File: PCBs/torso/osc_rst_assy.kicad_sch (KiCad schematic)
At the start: 8 parts, among them SW1 RESET

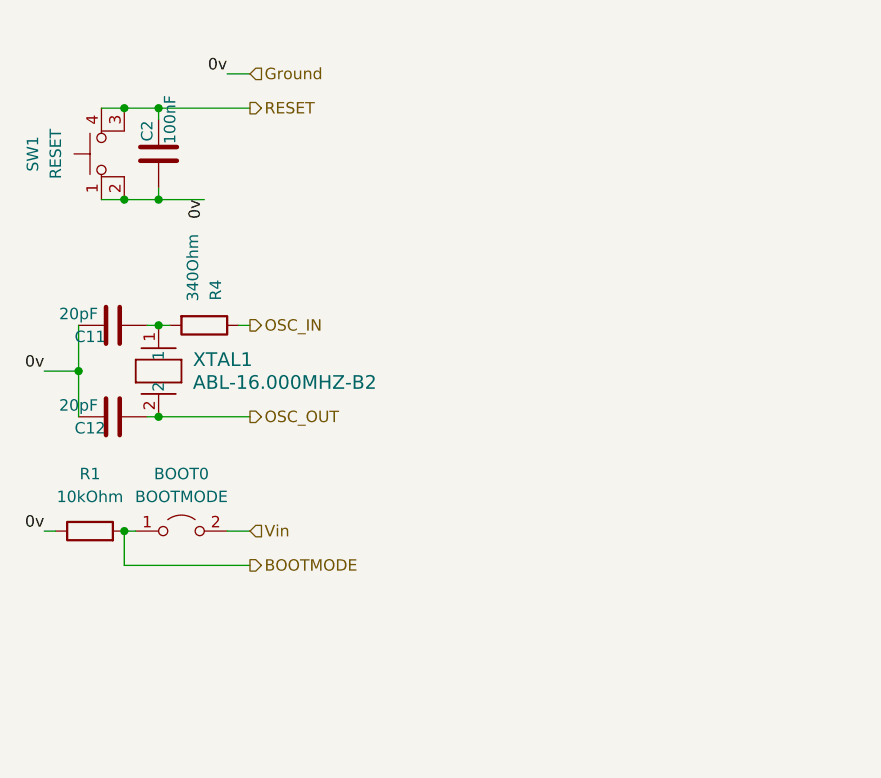
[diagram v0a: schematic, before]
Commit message: Torso all but complete, making bogie before checking the last mark
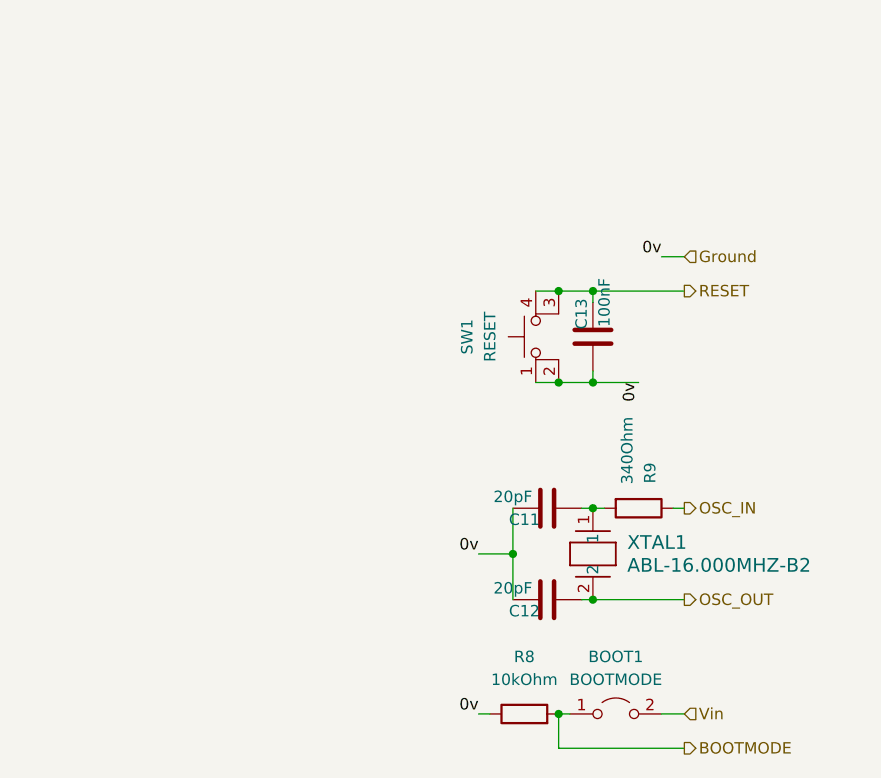
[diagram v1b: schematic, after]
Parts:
- removed BOOT0: BOOTMODE, Connector_PinHeader_2.54mm:PinHeader_1x02_P2.54mm_Vertical, symbol Jumper:Jumper_2_Open
- removed C2: 100nF, Capacitor_SMD:C_0603_1608Metric, symbol Device:C
- removed R1: 10kOhm, Resistor_SMD:R_0805_2012Metric, symbol Device:R
- removed R4: 340Ohm, Resistor_SMD:R_0805_2012Metric, symbol Device:R
- added BOOT1: BOOTMODE, Connector_PinHeader_2.54mm:PinHeader_1x02_P2.54mm_Vertical, symbol Jumper:Jumper_2_Open
- added C13: 100nF, Capacitor_SMD:C_0603_1608Metric, symbol Device:C
- added R8: 10kOhm, Resistor_SMD:R_0805_2012Metric, symbol Device:R
- added R9: 340Ohm, Resistor_SMD:R_0805_2012Metric, symbol Device:R
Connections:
- net BOOTMODE: now also BOOT1.1 (A), R8.2
- net Ground: now also C13.1, R8.1
- net OSC_IN: now also R9.1
- net RESET: now also C13.2
- net Vin: now also BOOT1.2 (B)
- net at C11.1, XTAL1.1: now also R9.2
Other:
- title: Oscillator and reset assembly -> (none)

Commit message: merged changes from timertests, mostly documentation and such. Did not add tim6 config
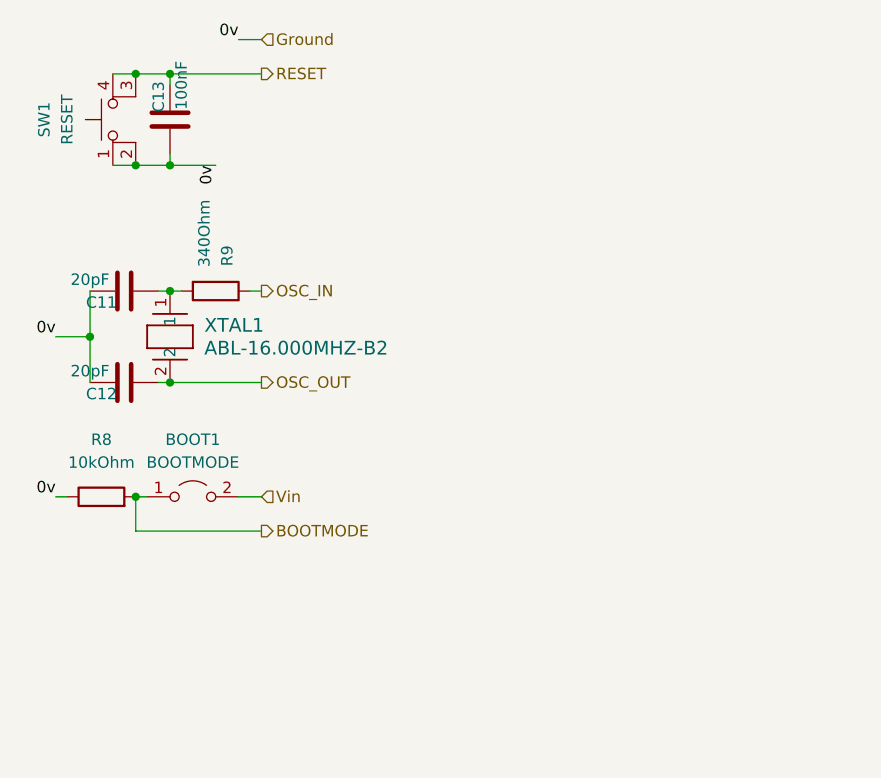
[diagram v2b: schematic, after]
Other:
- title: (none) -> Oscillator and reset assembly
- moved on the sheet: BOOT1, C11, C12, C13, R8, R9, SW1, XTAL1
